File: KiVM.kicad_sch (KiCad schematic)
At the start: 0 parts

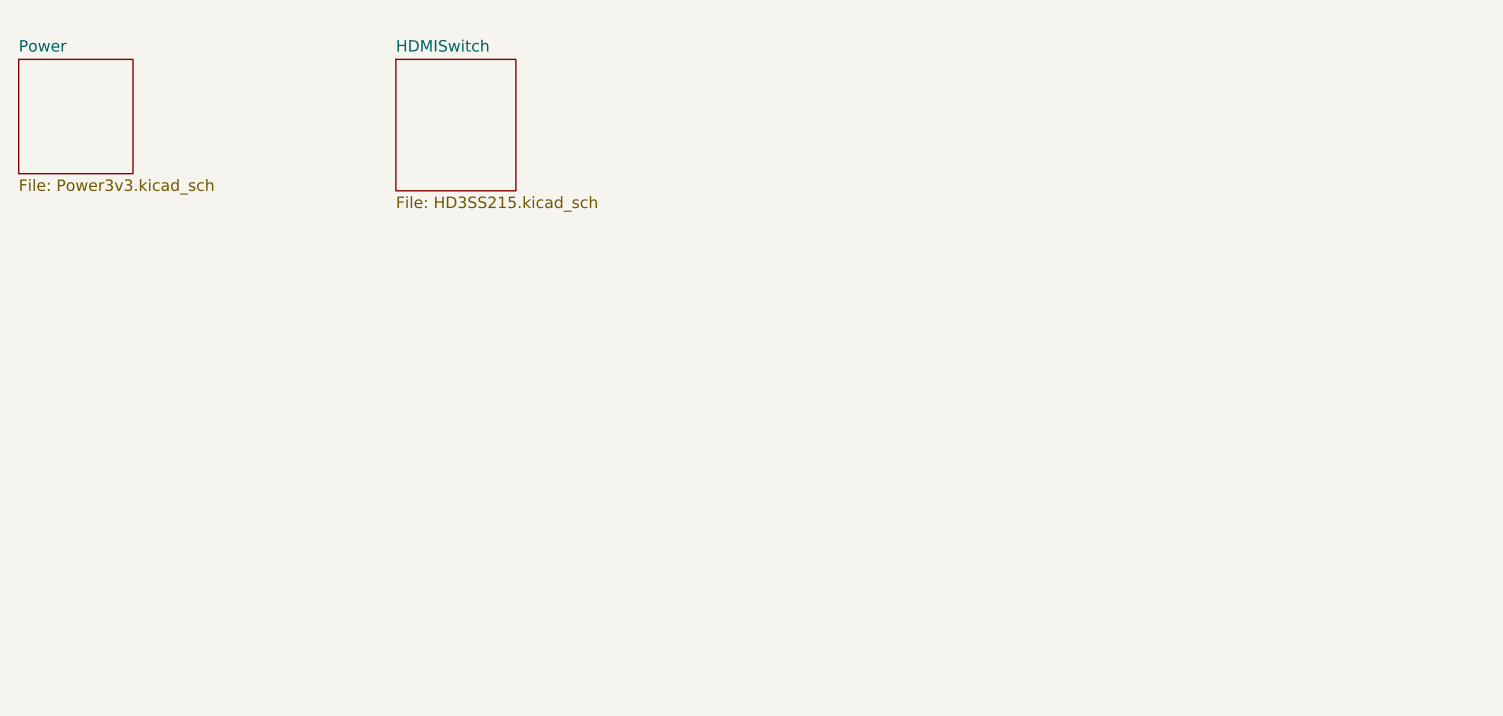
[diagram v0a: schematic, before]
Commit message: Only connectors left
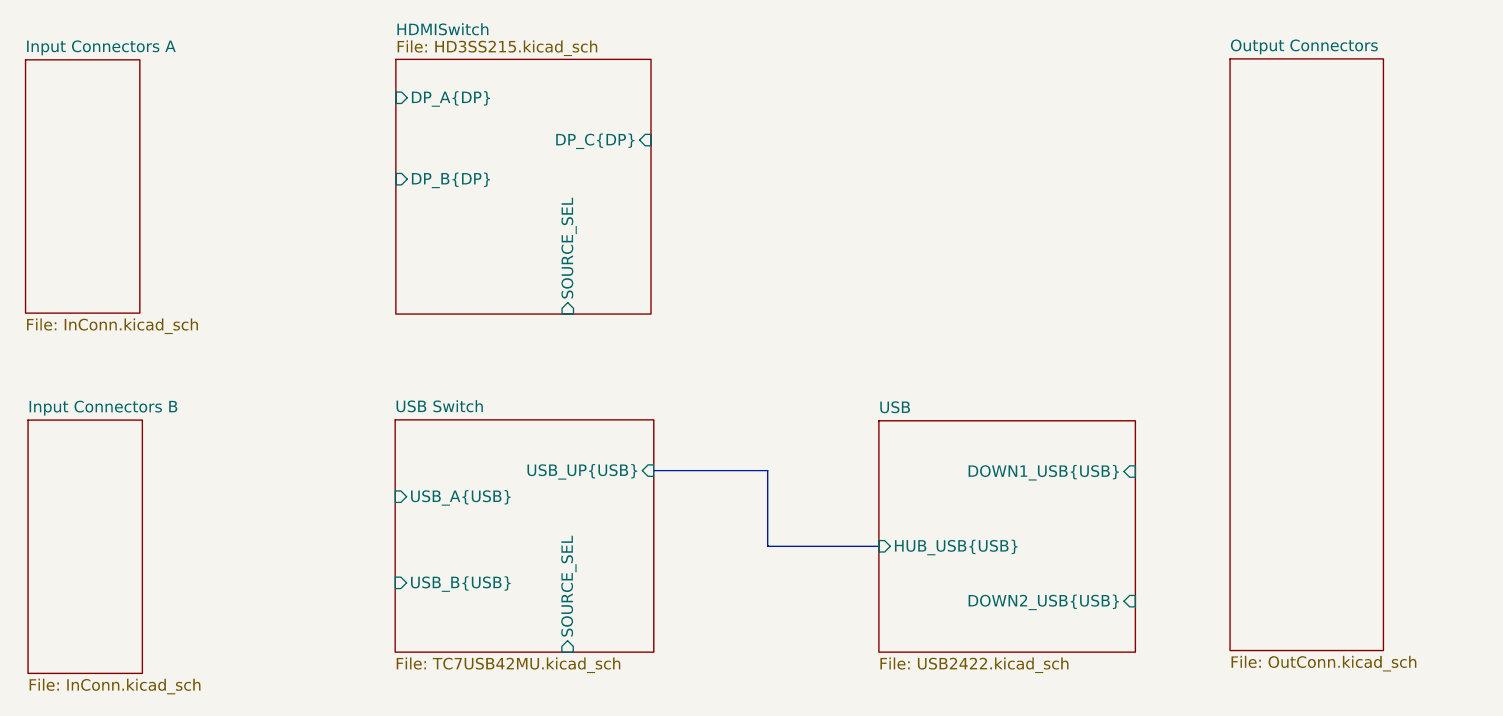
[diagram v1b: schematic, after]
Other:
- removed sheet Power
- added sheet Input Connectors A (InConn.kicad_sch)
- added sheet Input Connectors B (InConn.kicad_sch)
- added sheet Output Connectors (OutConn.kicad_sch)
- added sheet USB (USB2422.kicad_sch)
- added sheet USB Switch (TC7USB42MU.kicad_sch)
- sheet HDMISwitch ports: added DP_A{DP}, DP_B{DP}, DP_C{DP}, SOURCE_SEL; removed none

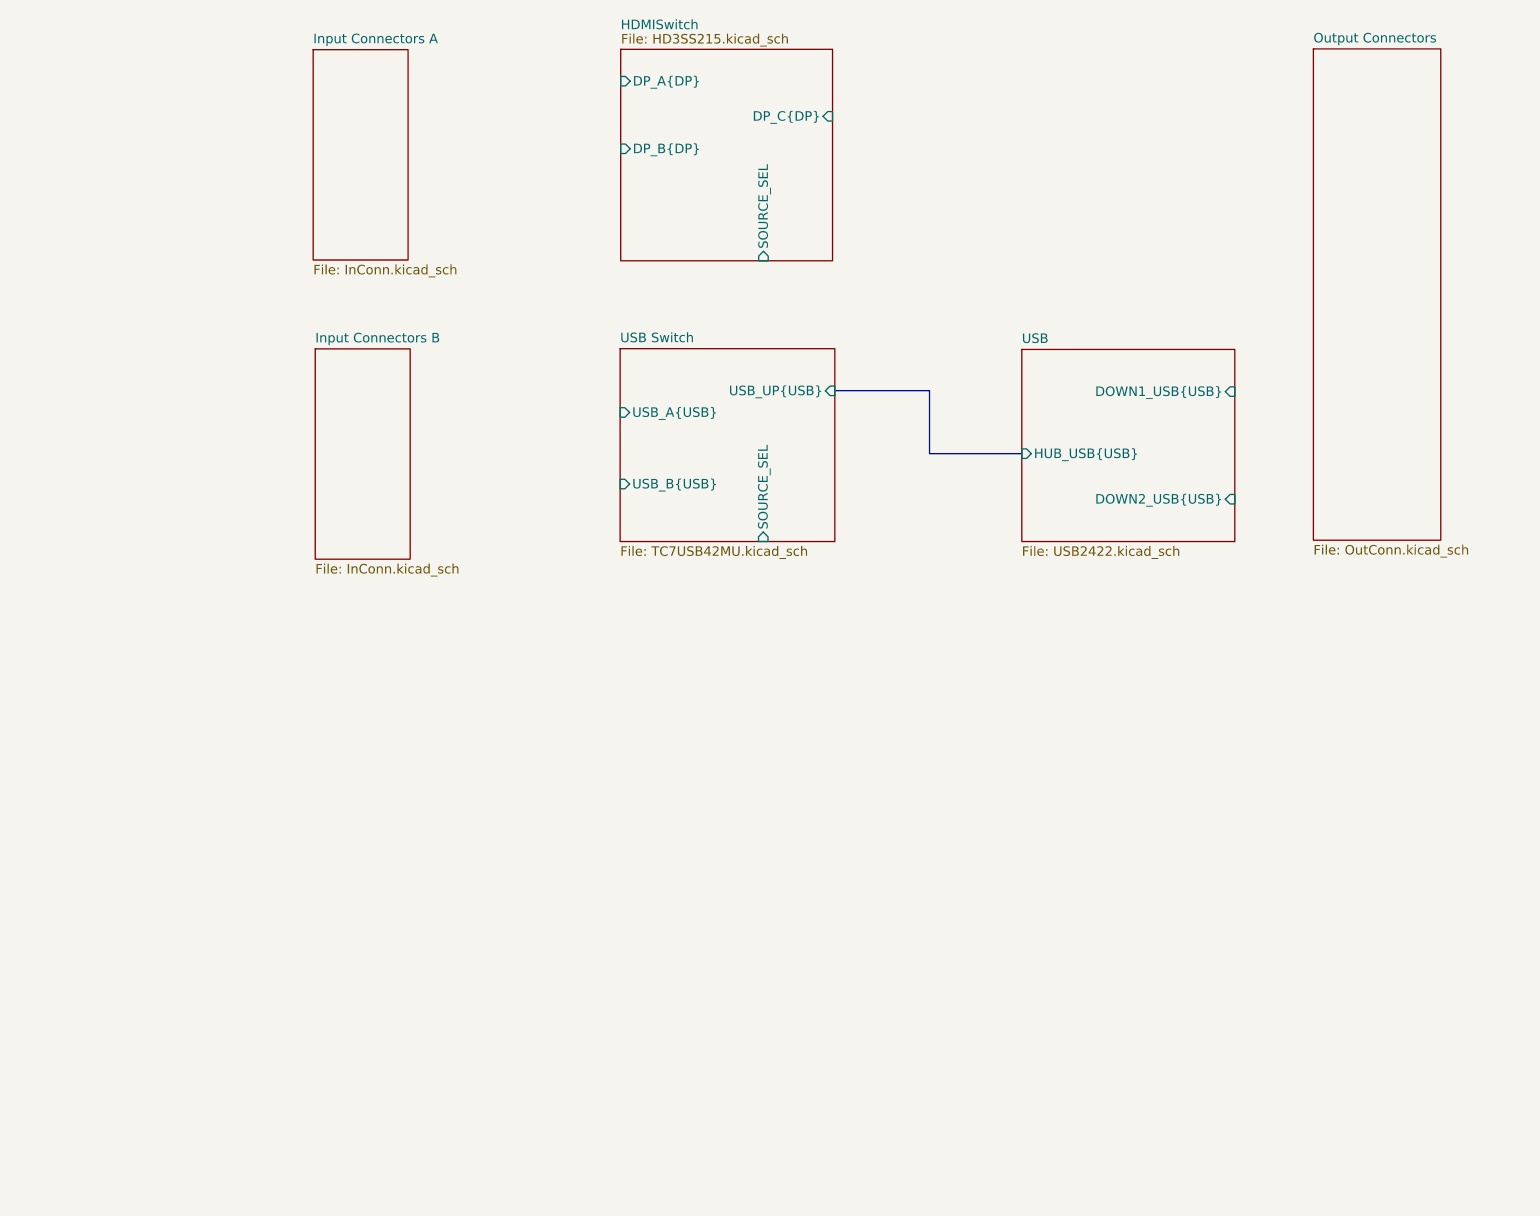
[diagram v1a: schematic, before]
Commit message: Adding 5v and 3v3 buck
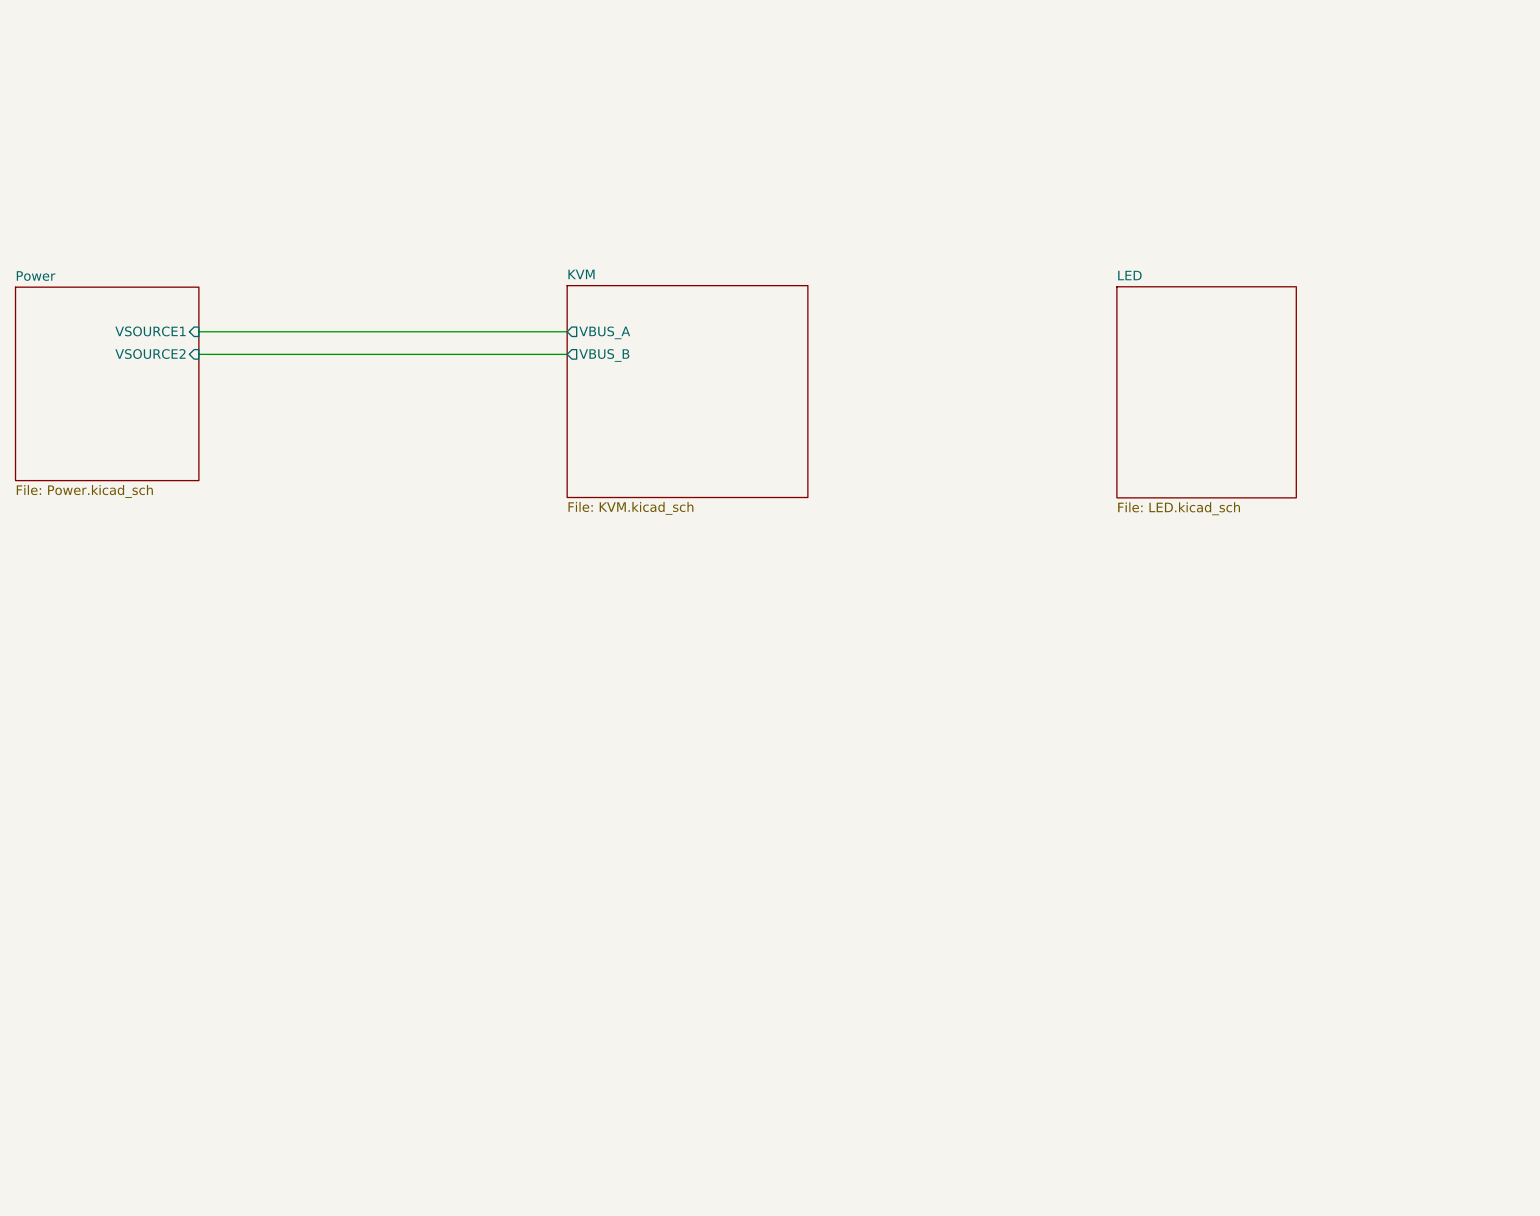
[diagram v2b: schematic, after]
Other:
- removed sheet HDMISwitch
- removed sheet Input Connectors A
- removed sheet Input Connectors B
- removed sheet Output Connectors
- removed sheet USB
- removed sheet USB Switch
- added sheet KVM (KVM.kicad_sch)
- added sheet LED (LED.kicad_sch)
- added sheet Power (Power.kicad_sch)

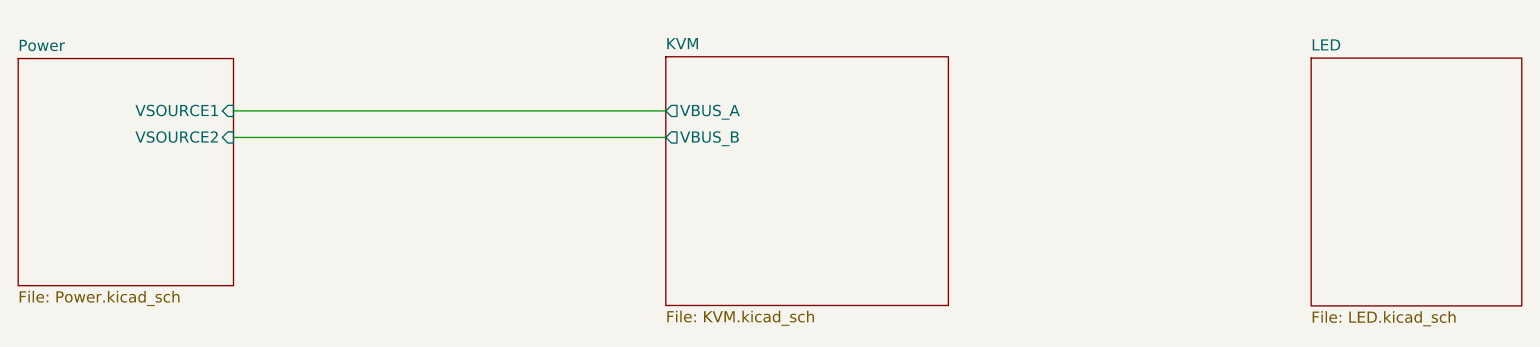
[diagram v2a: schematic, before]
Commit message: fixing sheet numbers and adding schematic PDF
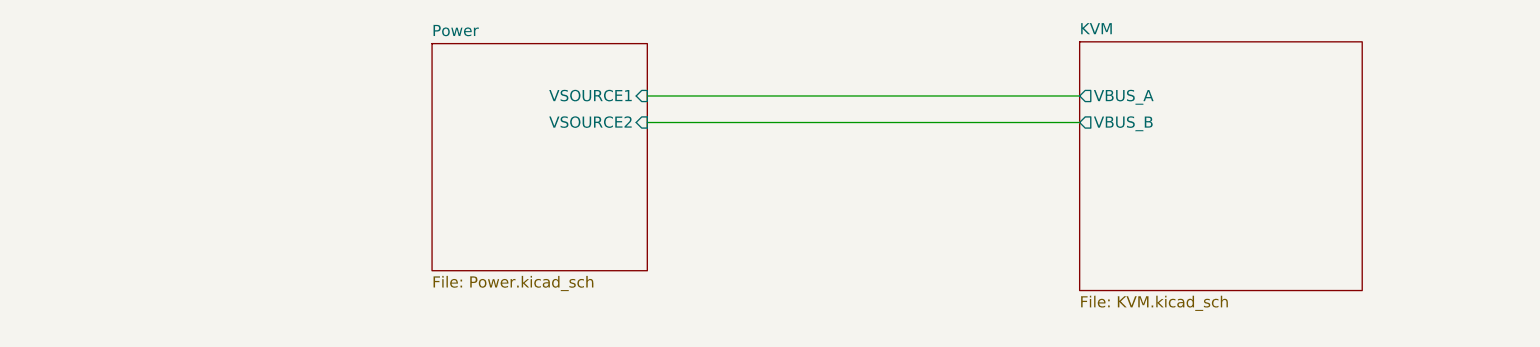
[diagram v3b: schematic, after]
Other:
- removed sheet LED

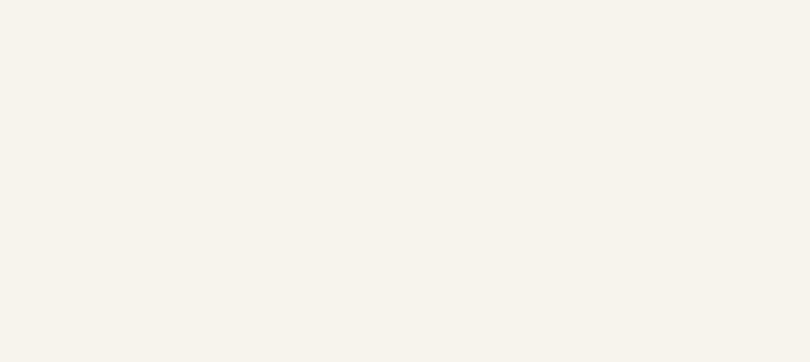
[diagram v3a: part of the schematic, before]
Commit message: Fixing ERC
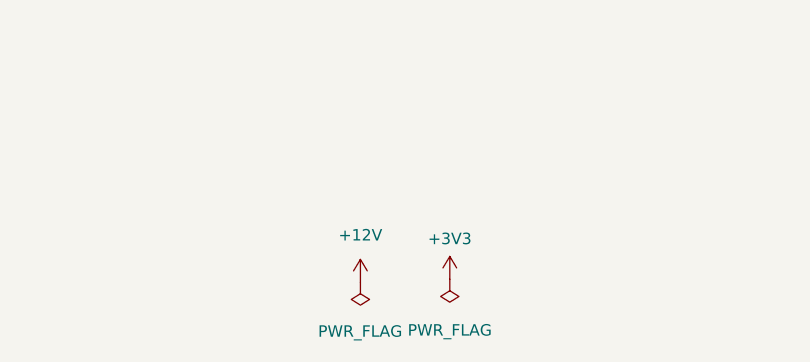
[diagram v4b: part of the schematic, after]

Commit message: Pushing what i have now
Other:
- sheet KVM ports: added none; removed VBUS_A, VBUS_B
- sheet Power: file Power.kicad_sch -> 5V0Power.kicad_sch
- sheet Power ports: added none; removed VSOURCE1, VSOURCE2
